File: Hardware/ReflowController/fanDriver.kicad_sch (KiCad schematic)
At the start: 1 part, among them U3 TB6612FNG

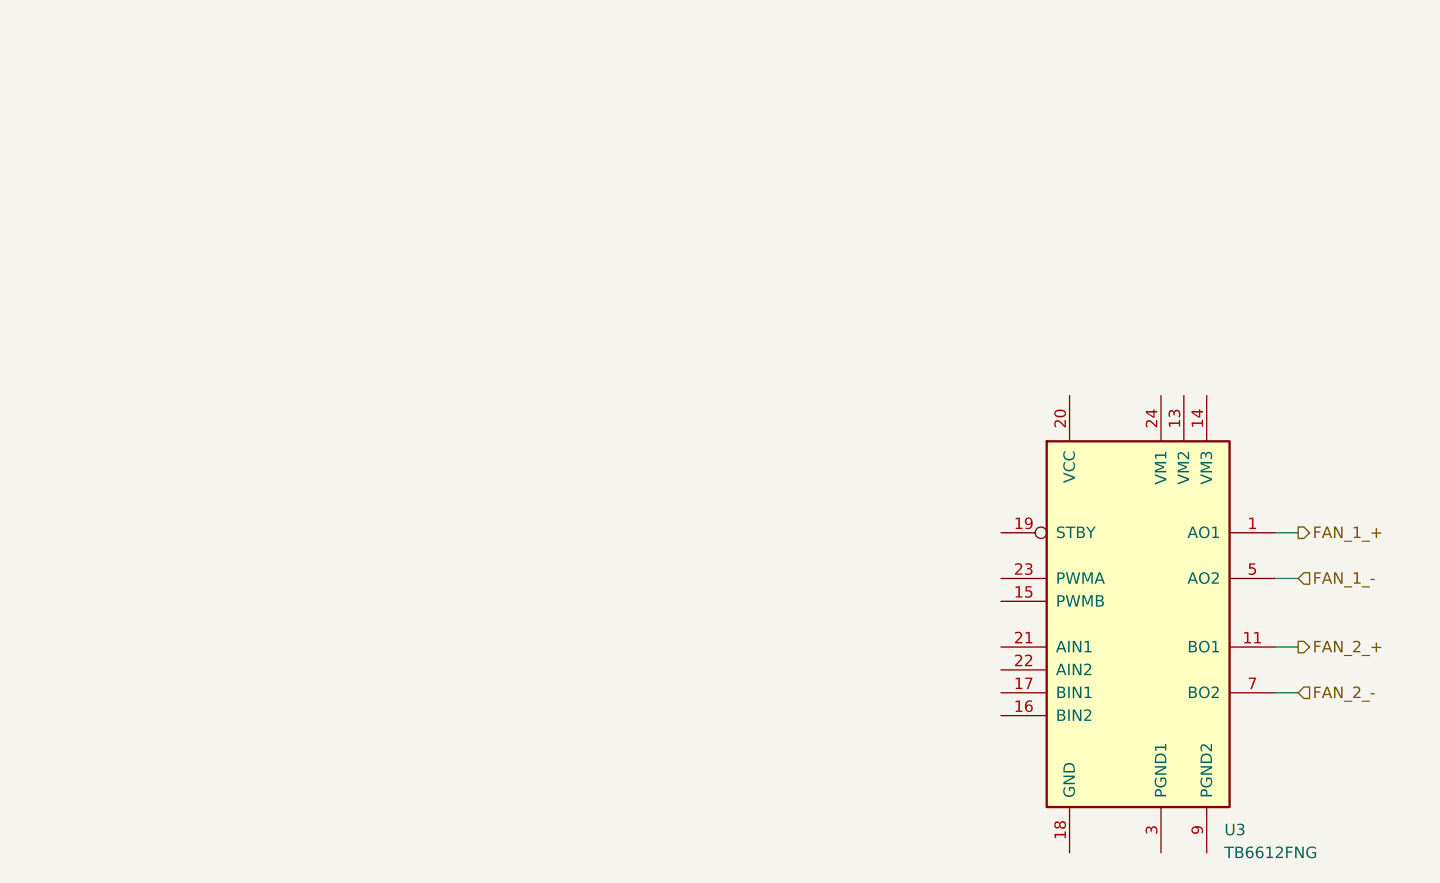
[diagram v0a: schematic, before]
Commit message: IMplemented the relay driver and High side switch. For the HSS there are some values to be caculated to enhance safety measures if we decide to implment them
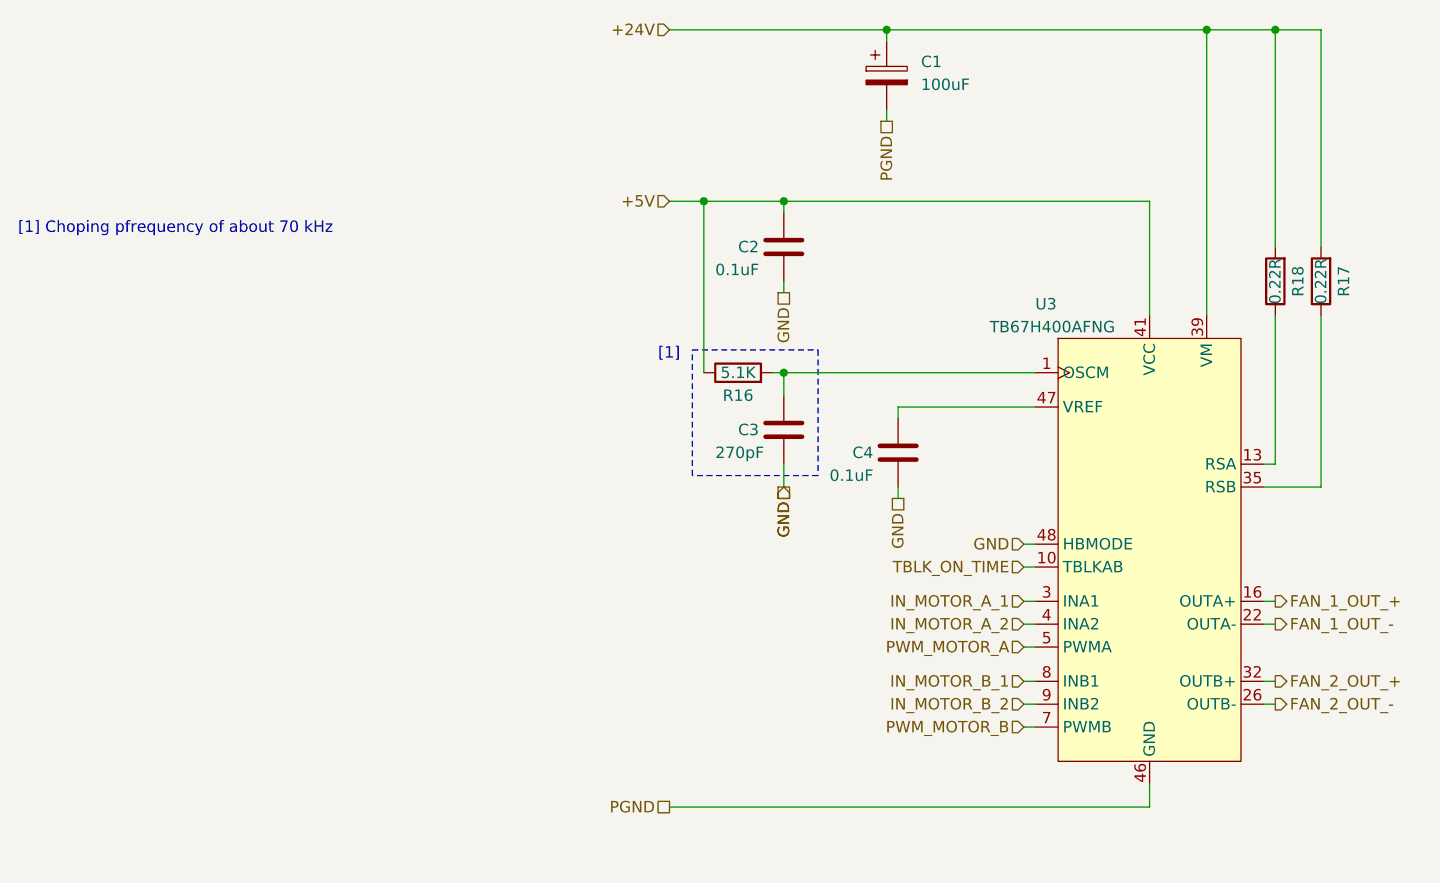
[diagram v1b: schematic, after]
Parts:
- removed U3: TB6612FNG, Package_SO:SSOP-24_5.3x8.2mm_P0.65mm, symbol Driver_Motor:TB6612FNG
- added C1: 100uF, symbol Device:C_Polarized
- added C2, C4: 0.1uF, symbol Device:C
- added C3: 270pF, symbol Device:C
- added R16: 5.1K, symbol Device:R
- added R17, R18: 0.22R, symbol Device:R
- added U3: TB67H400AFNG, 350_power_driver_motor_dc:HTSSOP48, symbol 350_power_driver_motor_dc:TB67H400AFNG,EL
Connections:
- new net: C3.1, R16.2, U3.1 (OSCM)
- new net: U3.12 (NC), U3.15 (NC), U3.18 (NC), U3.19 (NC), U3.2 (NC), U3.21 (NC), U3.28 (NC), U3.30 (NC), U3.31 (NC), U3.34 (NC), U3.37 (NC), U3.38 (NC), U3.40 (NC), U3.42 (NC), U3.43 (NC), U3.44 (NC), U3.45 (NC), U3.6 (NC)
- new net: R18.1, U3.13 (RSA), U3.14 (RSA)
- new net: R17.1, U3.35 (RSB), U3.36 (RSB)
- new net: C4.1, U3.47 (VREF)
- new net +24V: C1.1, R17.2, R18.2, U3.39 (VM)
- new net +5V: C2.1, R16.1, U3.41 (VCC)
- new net FAN_1_OUT_+: U3.16 (OUTA+), U3.17 (OUTA+)
- new net FAN_1_OUT_-: U3.22 (OUTA-), U3.23 (OUTA-)
- new net FAN_2_OUT_+: U3.32 (OUTB+), U3.33 (OUTB+)
- new net FAN_2_OUT_-: U3.26 (OUTB-), U3.27 (OUTB-)
- new net GND: C2.2, C3.2, C4.2, U3.48 (HBMODE)
- new net IN_MOTOR_A_1: U3.3 (INA1)
- new net IN_MOTOR_A_2: U3.4 (INA2)
- new net IN_MOTOR_B_1: U3.8 (INB1)
- new net IN_MOTOR_B_2: U3.9 (INB2)
- new net PGND: C1.2, U3.11 (GND), U3.20 (GND), U3.24 (GND), U3.25 (GND), U3.29 (GND), U3.46 (GND)
- new net PWM_MOTOR_A: U3.5 (PWMA)
- new net PWM_MOTOR_B: U3.7 (PWMB)
- new net TBLK_ON_TIME: U3.10 (TBLKAB)
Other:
- note added: "[1]"
- note added: "[1] Choping pfrequency of about 70 kHz"
